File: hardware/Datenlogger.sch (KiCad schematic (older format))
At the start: 57 parts, among them J1 AVR-ISP-6, J10 I2C0, J11 I2C1, J12 I2C2, J2 PWR, J3 Measure0, J4 Measure1, J5 serial, J6 SPI0, J7 SPI1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

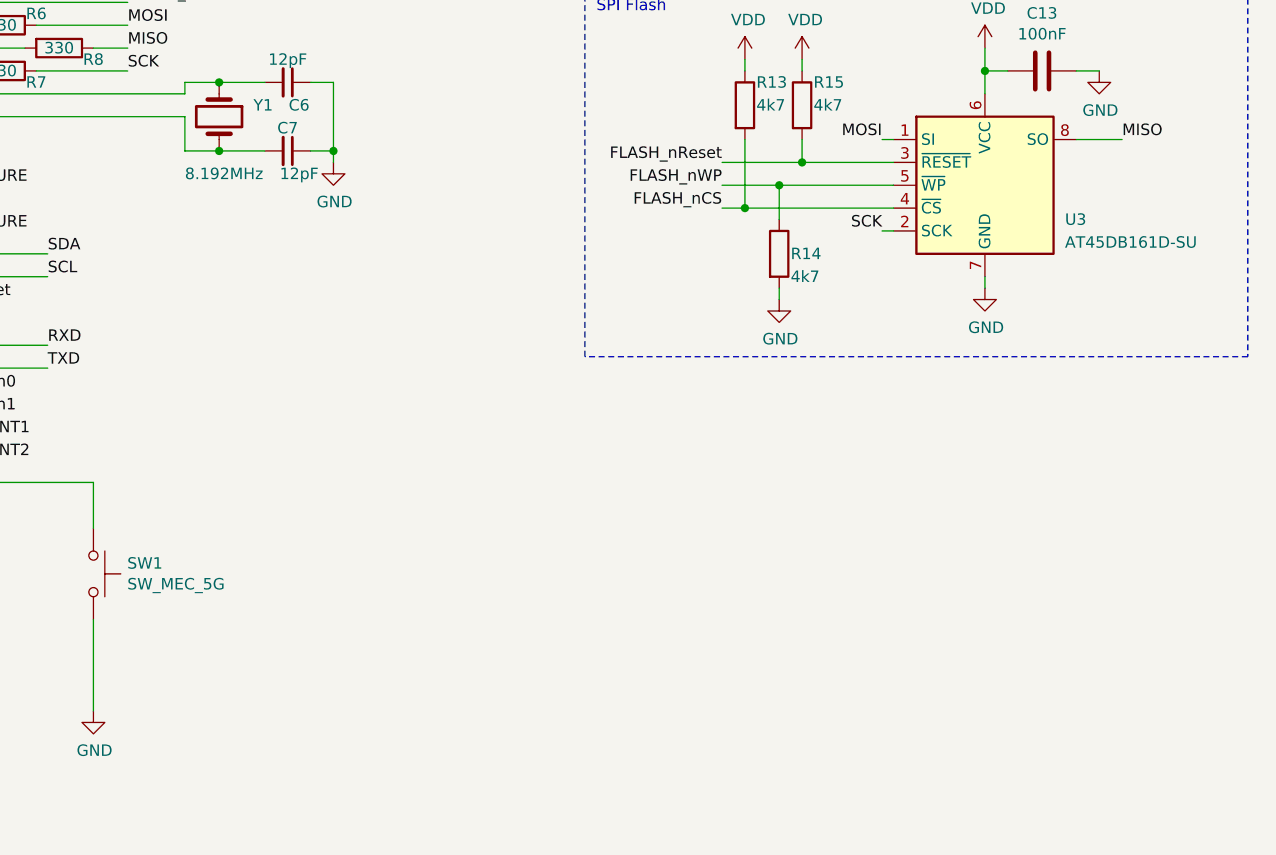
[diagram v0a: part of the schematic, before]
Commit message: Updated oscilator to be suited for standard UART baudrates.
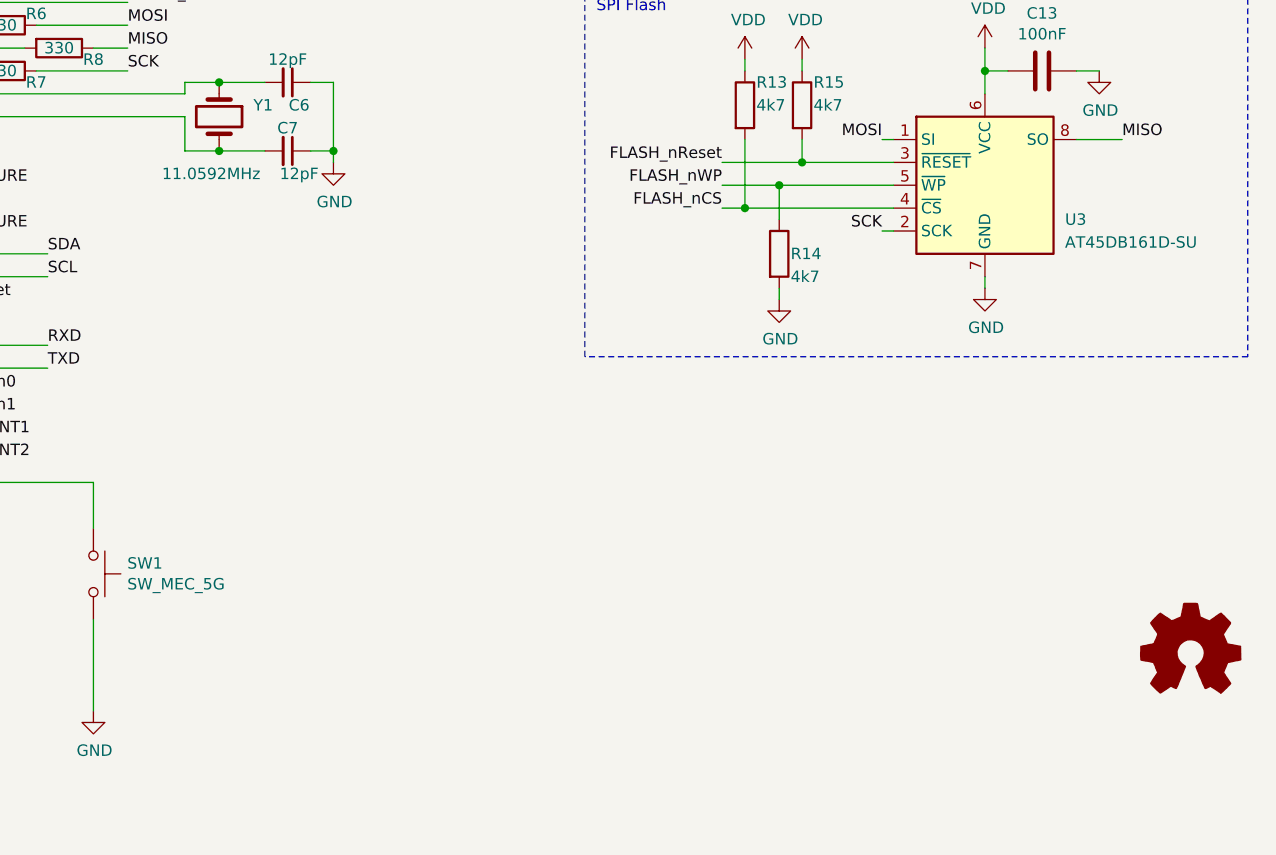
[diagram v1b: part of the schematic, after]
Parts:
- Y1: value 8.192MHz -> 11.0592MHz
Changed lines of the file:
@@
 P 6650 4500
 F 0 "Y1" V 6600 4650 50  0000 L CNN
-F 1 "8.192MHz" V 6900 4350 50  0000 L CNN
+F 1 "11.0592MHz" V 6900 4250 50  0000 L CNN
 F 2 "Crystal:Crystal_SMD_HC49-SD" H 6650 4500 50  0001 C CNN
 F 3 "~" H 6650 4500 50  0001 C CNN
@@
 Wire Wire Line
 	4700 1550 4700 1300
+$Comp
+L Graphic:Logo_Open_Hardware_Small #LOGO1
+U 1 1 60156491
+P 10900 6850
+F 0 "#LOGO1" H 10900 7125 50  0001 C CNN
+F 1 "Logo_Open_Hardware_Small" H 10900 6625 50  0001 C CNN
+F 2 "" H 10900 6850 50  0001 C CNN
+F 3 "~" H 10900 6850 50  0001 C CNN
+	1    10900 6850
+	1    0    0    -1
+$EndComp
 $EndSCHEMATC

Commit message: fix: Minor fixes to the hardware
Corrected text on allowed voltages to 2.6V-3.6V caused by the limits of the flash device.
Modified value of R1 to 56Ohm as the original was clearly way too high.

fixes #1
fixes #2
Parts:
- R1: value 1k -> 56
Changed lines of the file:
@@
 P 1500 2900
 F 0 "R1" H 1570 2946 50  0000 L CNN
-F 1 "1k" H 1570 2855 50  0000 L CNN
+F 1 "56" H 1570 2855 50  0000 L CNN
 F 2 "Resistor_SMD:R_0603_1608Metric_Pad0.98x0.95mm_HandSolder" V 1430 2900 50  0001 C CNN
 F 3 "~" H 1500 2900 50  0001 C CNN

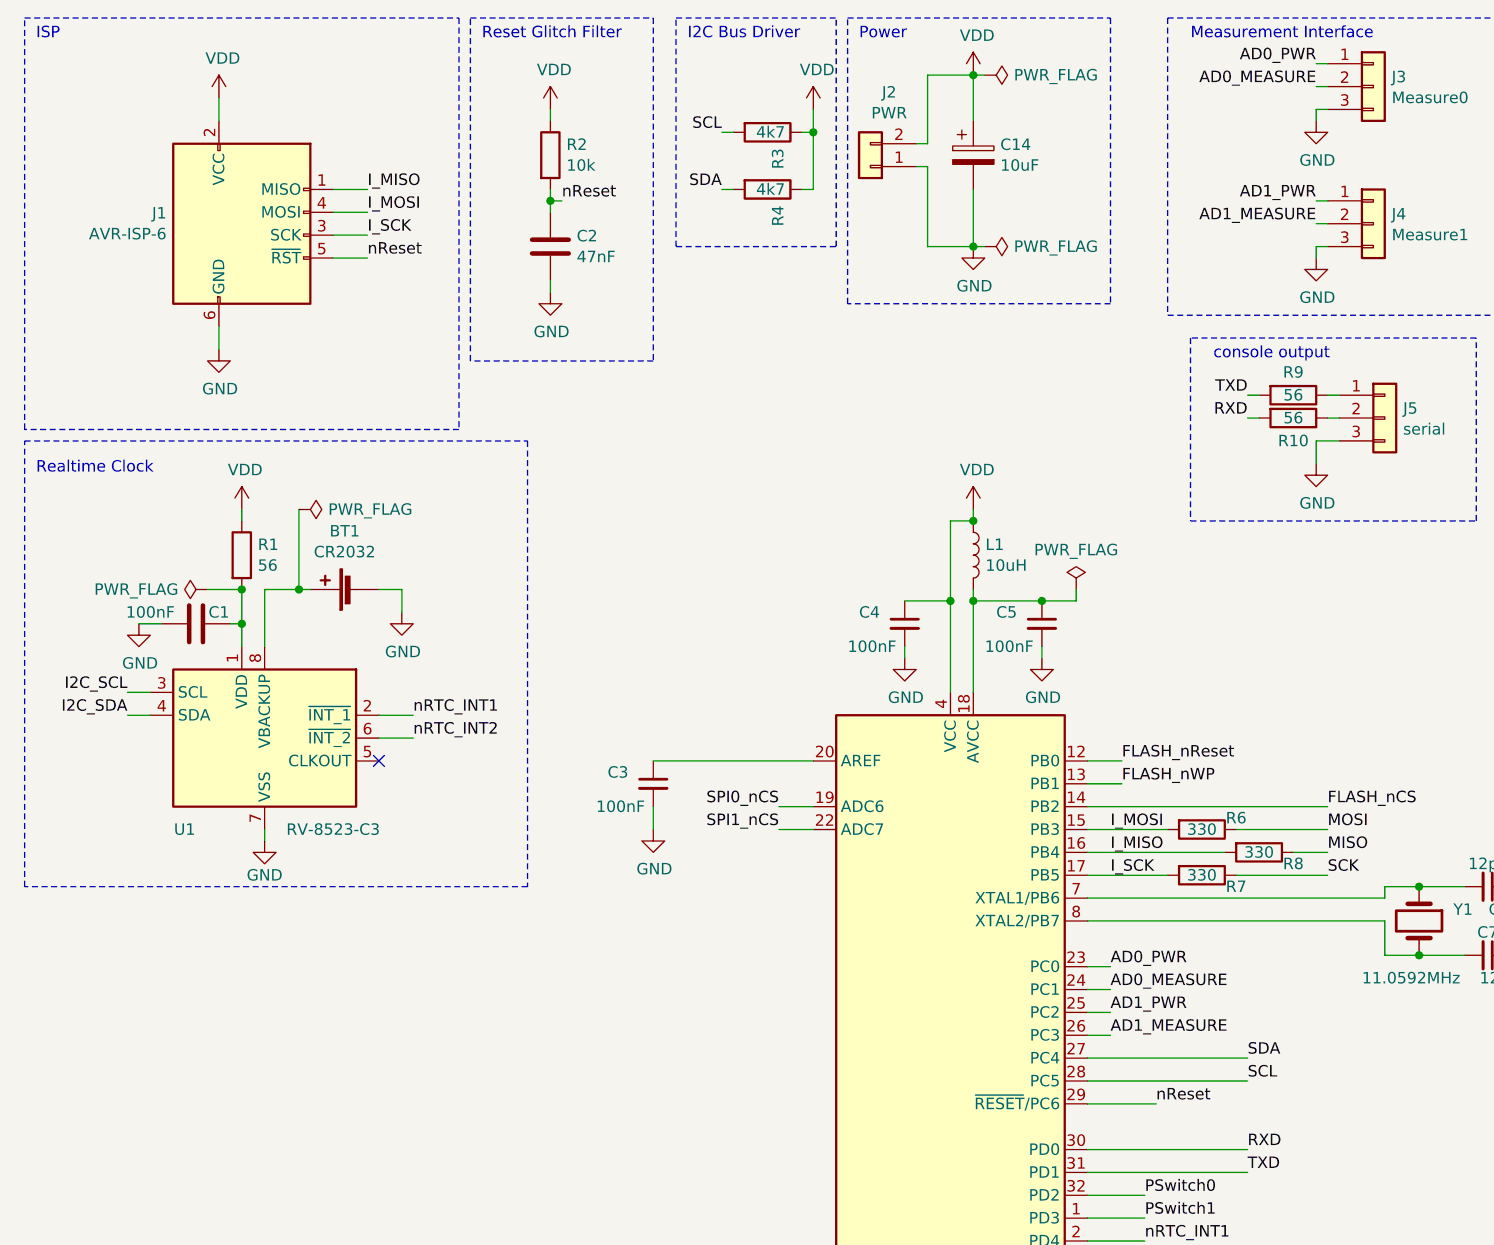
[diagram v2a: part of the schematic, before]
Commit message: Fundamental HW Fix, added testsuite
* fix #3  missing I2C connections
* fix #4  different components for R1/C1 to ensure switch-over to battery
* add extensive testsuite hwtest used to verify the HW.
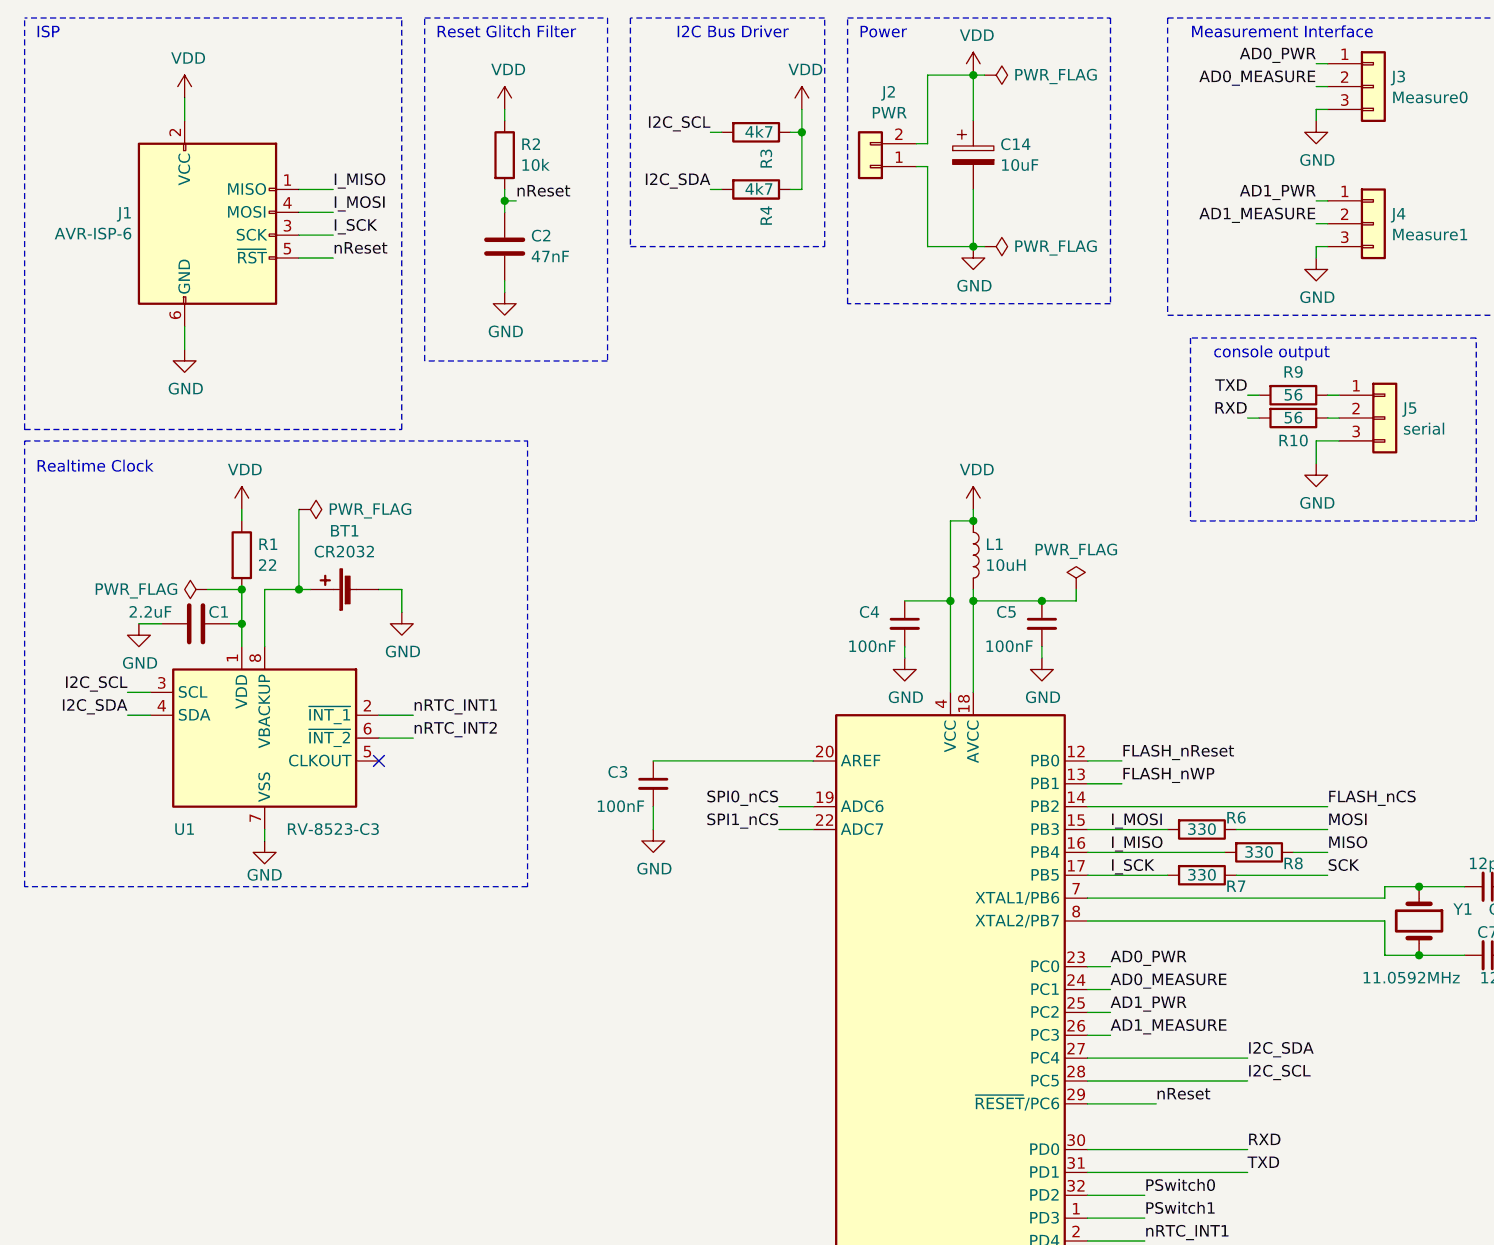
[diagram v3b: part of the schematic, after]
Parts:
- C1: value 100nF -> 2.2uF
- R1: value 56 -> 22
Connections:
- net SCL is gone; now on net I2C_SCL: R3.2, U2.28 (PC5)
- net SDA is gone; now on net I2C_SDA: R4.2, U2.27 (PC4)
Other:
- moved on the sheet: C2, J1, R2, R3, R4
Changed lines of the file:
@@
 Sheet 1 1
 Title "Datenlogger"
-Date "2021-01-25"
-Rev "1.0"
+Date "2021-04-07"
+Rev "1.1"
 Comp "Michael Staudenmaier"
 Comment1 ""
@@
 L power:VDD #PWR04
 U 1 1 5ECDE6DC
-P 1400 900
-F 0 "#PWR04" H 1400 750 50  0001 C CNN
-F 1 "VDD" H 1417 1073 50  0000 C CNN
-F 2 "" H 1400 900 50  0001 C CNN
-F 3 "" H 1400 900 50  0001 C CNN
-	1    1400 900
+P 1250 900
+F 0 "#PWR04" H 1250 750 50  0001 C CNN
+F 1 "VDD" H 1267 1073 50  0000 C CNN
+F 2 "" H 1250 900 50  0001 C CNN
+F 3 "" H 1250 900 50  0001 C CNN
+	1    1250 900
 	1    0    0    -1
 $EndComp
@@
 L power:GND #PWR05
 U 1 1 5ECDE711
-P 1400 2000
-F 0 "#PWR05" H 1400 1750 50  0001 C CNN
-F 1 "GND" H 1405 1827 50  0000 C CNN
-F 2 "" H 1400 2000 50  0001 C CNN
-F 3 "" H 1400 2000 50  0001 C CNN
-	1    1400 2000
-	1    0    0    -1
-$EndComp
-Wire Wire Line
-	1400 1000 1400 900
-Wire Wire Line
-	1400 2000 1400 1900
-Text Label 2050 1300 0    50   ~ 0
+P 1250 2000
+F 0 "#PWR05" H 1250 1750 50  0001 C CNN
+F 1 "GND" H 1255 1827 50  0000 C CNN
+F 2 "" H 1250 2000 50  0001 C CNN
+F 3 "" H 1250 2000 50  0001 C CNN
+	1    1250 2000
+	1    0    0    -1
+$EndComp
+Wire Wire Line
+	1250 1000 1250 900
+Wire Wire Line
+	1250 2000 1250 1900
+Text Label 1900 1300 0    50   ~ 0
 I_MISO
-Text Label 2050 1400 0    50   ~ 0
+Text Label 1900 1400 0    50   ~ 0
 I_MOSI
-Text Label 2050 1500 0    50   ~ 0
+Text Label 1900 1500 0    50   ~ 0
 I_SCK
-Text Label 2050 1600 0    50   ~ 0
+Text Label 1900 1600 0    50   ~ 0
 nReset
 Wire Wire Line
-	1900 1300 2050 1300
-Wire Wire Line
-	1900 1400 2050 1400
-Wire Wire Line
-	1900 1500 2050 1500
-Wire Wire Line
-	1900 1600 2050 1600
+	1750 1300 1900 1300
+Wire Wire Line
+	1750 1400 1900 1400
+Wire Wire Line
+	1750 1500 1900 1500
+Wire Wire Line
+	1750 1600 1900 1600
 Text Label 5350 3800 0    50   ~ 0
 FLASH_nReset
@@
 	5200 5800 5450 5800
 Text Label 5900 5100 0    50   ~ 0
-SDA
+I2C_SDA
 Text Label 5900 5200 0    50   ~ 0
-SCL
+I2C_SCL
 Wire Wire Line
 	5200 5100 5900 5100
@@
 L Device:R R3
 U 1 1 5ED52A03
-P 3800 1050
-F 0 "R3" H 3870 1096 50  0000 L CNN
-F 1 "4k7" V 3800 1000 50  0000 L CNN
-F 2 "Resistor_SMD:R_0603_1608Metric_Pad0.98x0.95mm_HandSolder" V 3730 1050 50  0001 C CNN
-F 3 "~" H 3800 1050 50  0001 C CNN
-	1    3800 1050
+P 3750 1050
+F 0 "R3" H 3820 1096 50  0000 L CNN
+F 1 "4k7" V 3750 1000 50  0000 L CNN
+F 2 "Resistor_SMD:R_0603_1608Metric_Pad0.98x0.95mm_HandSolder" V 3680 1050 50  0001 C CNN
+F 3 "~" H 3750 1050 50  0001 C CNN
+	1    3750 1050
 	0    1    1    0
 $EndComp
@@
 L Device:R R4
 U 1 1 5ED52F1F
-P 3800 1300
-F 0 "R4" H 3870 1346 50  0000 L CNN
-F 1 "4k7" V 3800 1250 50  0000 L CNN
-F 2 "Resistor_SMD:R_0603_1608Metric_Pad0.98x0.95mm_HandSolder" V 3730 1300 50  0001 C CNN
-F 3 "~" H 3800 1300 50  0001 C CNN
-	1    3800 1300
+P 3750 1300
+F 0 "R4" H 3820 1346 50  0000 L CNN
+F 1 "4k7" V 3750 1250 50  0000 L CNN
+F 2 "Resistor_SMD:R_0603_1608Metric_Pad0.98x0.95mm_HandSolder" V 3680 1300 50  0001 C CNN
+F 3 "~" H 3750 1300 50  0001 C CNN
+	1    3750 1300
 	0    1    1    0
 $EndComp
@@
 L power:VDD #PWR014
 U 1 1 5EDA27F8
-P 4000 950
-F 0 "#PWR014" H 4000 800 50  0001 C CNN
-F 1 "VDD" H 4017 1123 50  0000 C CNN
-F 2 "" H 4000 950 50  0001 C CNN
-F 3 "" H 4000 950 50  0001 C CNN
-	1    4000 950
-	1    0    0    -1
-$EndComp
-Text Label 3600 1050 2    50   ~ 0
-SCL
-Text Label 3600 1300 2    50   ~ 0
-SDA
-Wire Notes Line
-	3400 1550 3400 550
-Text Notes 3450 650  0    50   ~ 0
+P 3950 950
+F 0 "#PWR014" H 3950 800 50  0001 C CNN
+F 1 "VDD" H 3967 1123 50  0000 C CNN
+F 2 "" H 3950 950 50  0001 C CNN
+F 3 "" H 3950 950 50  0001 C CNN
+	1    3950 950
+	1    0    0    -1
+$EndComp
+Text Label 3550 1050 2    50   ~ 0
+I2C_SCL
+Text Label 3550 1300 2    50   ~ 0
+I2C_SDA
+Text Notes 3400 650  0    50   ~ 0
 I2C Bus Driver
-Wire Notes Line
-	550  550  2450 550
-Wire Notes Line
-	2450 550  2450 2350
-Wire Notes Line
-	2450 2350 550  2350
 Wire Notes Line
 	550  2350 550  550
@@
 L Connector:AVR-ISP-6 J1
 U 1 1 60108C51
-P 1500 1500
-F 0 "J1" H 1171 1596 50  0000 R CNN
-F 1 "AVR-ISP-6" H 1171 1505 50  0000 R CNN
-F 2 "Connector_PinHeader_2.54mm:PinHeader_2x03_P2.54mm_Vertical" V 1250 1550 50  0001 C CNN
-F 3 " ~" H 225 950 50  0001 C CNN
-	1    1500 1500
+P 1350 1500
+F 0 "J1" H 1021 1596 50  0000 R CNN
+F 1 "AVR-ISP-6" H 1021 1505 50  0000 R CNN
+F 2 "Connector_PinHeader_2.54mm:PinHeader_2x03_P2.54mm_Vertical" V 1100 1550 50  0001 C CNN
+F 3 " ~" H 75  950 50  0001 C CNN
+	1    1350 1500
 	1    0    0    -1
 $EndComp
@@
 P 1300 3200
 F 0 "C1" V 1250 3300 50  0000 C CNN
-F 1 "100nF" V 1250 3000 50  0000 C CNN
+F 1 "2.2uF" V 1250 3000 50  0000 C CNN
 F 2 "Capacitor_SMD:C_0603_1608Metric_Pad1.08x0.95mm_HandSolder" H 1338 3050 50  0001 C CNN
 F 3 "~" H 1300 3200 50  0001 C CNN
@@
 P 1500 2900
 F 0 "R1" H 1570 2946 50  0000 L CNN
-F 1 "56" H 1570 2855 50  0000 L CNN
+F 1 "22" H 1570 2855 50  0000 L CNN
 F 2 "Resistor_SMD:R_0603_1608Metric_Pad0.98x0.95mm_HandSolder" V 1430 2900 50  0001 C CNN
 F 3 "~" H 1500 2900 50  0001 C CNN
@@
 L Device:R R2
 U 1 1 601E8F51
-P 2850 1150
-F 0 "R2" H 2920 1196 50  0000 L CNN
-F 1 "10k" H 2920 1105 50  0000 L CNN
-F 2 "Resistor_SMD:R_0603_1608Metric_Pad0.98x0.95mm_HandSolder" V 2780 1150 50  0001 C CNN
-F 3 "~" H 2850 1150 50  0001 C CNN
-	1    2850 1150
+P 2650 1150
+F 0 "R2" H 2720 1196 50  0000 L CNN
+F 1 "10k" H 2720 1105 50  0000 L CNN
+F 2 "Resistor_SMD:R_0603_1608Metric_Pad0.98x0.95mm_HandSolder" V 2580 1150 50  0001 C CNN
+F 3 "~" H 2650 1150 50  0001 C CNN
+	1    2650 1150
 	1    0    0    -1
 $EndComp
@@
 L power:VDD #PWR011
 U 1 1 601E9457
-P 2850 950
-F 0 "#PWR011" H 2850 800 50  0001 C CNN
-F 1 "VDD" H 2867 1123 50  0000 C CNN
-F 2 "" H 2850 950 50  0001 C CNN
-F 3 "" H 2850 950 50  0001 C CNN
-	1    2850 950
+P 2650 950
+F 0 "#PWR011" H 2650 800 50  0001 C CNN
+F 1 "VDD" H 2667 1123 50  0000 C CNN
+F 2 "" H 2650 950 50  0001 C CNN
+F 3 "" H 2650 950 50  0001 C CNN
+	1    2650 950
 	1    0    0    -1
 $EndComp
@@
 L Device:C C2
 U 1 1 601E9DB5
-P 2850 1550
-F 0 "C2" H 2965 1596 50  0000 L CNN
-F 1 "47nF" H 2965 1505 50  0000 L CNN
-F 2 "Capacitor_SMD:C_0603_1608Metric_Pad1.08x0.95mm_HandSolder" H 2888 1400 50  0001 C CNN
-F 3 "~" H 2850 1550 50  0001 C CNN
-	1    2850 1550
+P 2650 1550
+F 0 "C2" H 2765 1596 50  0000 L CNN
+F 1 "47nF" H 2765 1505 50  0000 L CNN
+F 2 "Capacitor_SMD:C_0603_1608Metric_Pad1.08x0.95mm_HandSolder" H 2688 1400 50  0001 C CNN
+F 3 "~" H 2650 1550 50  0001 C CNN
+	1    2650 1550
 	1    0    0    -1
 $EndComp
@@
 L power:GND #PWR012
 U 1 1 601EA412
-P 2850 1750
-F 0 "#PWR012" H 2850 1500 50  0001 C CNN
-F 1 "GND" H 2855 1577 50  0000 C CNN
-F 2 "" H 2850 1750 50  0001 C CNN
-F 3 "" H 2850 1750 50  0001 C CNN
-	1    2850 1750
-	1    0    0    -1
-$EndComp
-Wire Wire Line
-	2850 1400 2850 1350
-Wire Wire Line
-	2850 1750 2850 1700
-Text Label 2900 1350 0    50   ~ 0
+P 2650 1750
+F 0 "#PWR012" H 2650 1500 50  0001 C CNN
+F 1 "GND" H 2655 1577 50  0000 C CNN
+F 2 "" H 2650 1750 50  0001 C CNN
+F 3 "" H 2650 1750 50  0001 C CNN
+	1    2650 1750
+	1    0    0    -1
+$EndComp
+Wire Wire Line
+	2650 1400 2650 1350
+Wire Wire Line
+	2650 1750 2650 1700
+Text Label 2700 1350 0    50   ~ 0
 nReset
 Wire Wire Line
-	2850 1350 2900 1350
-Connection ~ 2850 1350
-Wire Wire Line
-	2850 1350 2850 1300
-Wire Wire Line
-	2850 1000 2850 950
-Wire Notes Line
-	2500 2050 2500 550
-Wire Notes Line
-	2500 550  3300 550
-Wire Notes Line
-	3300 550  3300 2050
-Wire Notes Line
-	3300 2050 2500 2050
-Text Notes 2550 650  0    50   ~ 0
+	2650 1350 2700 1350
+Connection ~ 2650 1350
+Wire Wire Line
+	2650 1350 2650 1300
+Wire Wire Line
+	2650 1000 2650 950
+Wire Notes Line
+	2300 2050 2300 550
+Wire Notes Line
+	2300 550  3100 550
+Wire Notes Line
+	3100 550  3100 2050
+Wire Notes Line
+	3100 2050 2300 2050
+Text Notes 2350 650  0    50   ~ 0
 Reset Glitch Filter
 Wire Wire Line
@@
 	6200 950  6250 950
 Wire Wire Line
-	3600 1050 3650 1050
-Wire Wire Line
-	3600 1300 3650 1300
-Wire Wire Line
-	4000 950  4000 1050
-Wire Wire Line
-	3950 1300 4000 1300
-Wire Wire Line
-	4000 1050 3950 1050
-Connection ~ 4000 1050
-Wire Wire Line
-	4000 1050 4000 1300
-Wire Notes Line
-	4100 1550 4100 550
-Wire Notes Line
-	3400 550  4100 550
-Wire Notes Line
-	3400 1550 4100 1550
+	3550 1050 3600 1050
+Wire Wire Line
+	3550 1300 3600 1300
+Wire Wire Line
+	3950 950  3950 1050
+Wire Wire Line
+	3900 1300 3950 1300
+Wire Wire Line
+	3950 1050 3900 1050
+Connection ~ 3950 1050
+Wire Wire Line
+	3950 1050 3950 1300
+Wire Notes Line
+	4050 1550 4050 550
 $Comp
 L Connector_Generic:Conn_01x03 J4
@@
 	1    0    0    -1
 $EndComp
+Wire Notes Line
+	550  2350 2200 2350
+Wire Notes Line
+	2200 2350 2200 550
+Wire Notes Line
+	2200 550  550  550
+Wire Notes Line
+	4050 550  3200 550
+Wire Notes Line
+	3200 550  3200 1550
+Wire Notes Line
+	3200 1550 4050 1550
 $EndSCHEMATC
